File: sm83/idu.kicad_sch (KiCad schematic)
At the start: 48 parts

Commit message: SM83: Add schematic for interrupt handling
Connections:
- new net: IDU1. (CHAIN_A_~{Y}), IDU_MUX_L1.
- new net: IDU0. (ZERO_Y), IDU_MUX_L0.
- new net: IDU2. (CHAIN_A_~{Y}), IDU_MUX_L2.
- new net: IDU6. (CHAIN_A_~{Y}), IDU_MUX_H6.
- new net: IDU3. (CHAIN_A_~{Y}), IDU_MUX_L3.
- new net: IDU0. (ZERO_Y), IDU_MUX_L7.
- new net: IDU3. (CHAIN_A_~{Y}), IDU_MUX_H3.
- new net: IDU2. (CHAIN_A_~{Y}), IDU3. (CHAIN_A_~{Y}) (x2)
- new net: IDU3. (CHAIN_A_~{Y}), IDU4. (CHAIN_A_~{Y}) (x2)
- new net: IDU2. (CHAIN_A_~{Y}), IDU_MUX_H2.
- new net: IDU0. (ZERO_Y), IDU_MUX_H0.
- new net: IDU1. (CHAIN_A_~{Y}), IDU_MUX_H1.
- new net: IDU4. (CHAIN_A_~{Y}), IDU_MUX_L4.
- new net: IDU1. (CHAIN_A_~{Y}), IDU2. (CHAIN_A_~{Y}) (x2)
- new net: IDU6. (CHAIN_A_~{Y}), IDU_MUX_L6.
- new net: IDU0. (ZERO_Y), IDU1. (CHAIN_A_~{Y}) (x2)
- new net: IDU5. (CHAIN_A_~{Y}), IDU6. (CHAIN_A_~{Y}) (x2)
- new net: IDU6. (CHAIN_A_~{Y}), IDU7. (NOT_A_Y) (x2)
- new net: IDU4. (CHAIN_A_~{Y}), IDU_MUX_H4.
- new net: IDU4. (CHAIN_A_~{Y}), IDU5. (CHAIN_A_~{Y}) (x2)
- new net: IDU5. (CHAIN_A_~{Y}), IDU_MUX_H5.
- new net: IDU5. (CHAIN_A_~{Y}), IDU_MUX_L5.

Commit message: Finish SM83 CPU schematic
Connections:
- new net: IDU1. (CHAIN_A_~{Y}), IDU_MUX_L1.
- new net: IDU0. (ZERO_Y), IDU_MUX_L0.
- new net: IDU2. (CHAIN_A_~{Y}), IDU_MUX_L2.
- new net: IDU6. (CHAIN_A_~{Y}), IDU_MUX_H6.
- new net: IDU3. (CHAIN_A_~{Y}), IDU_MUX_L3.
- new net: IDU0. (ZERO_Y), IDU_MUX_L7.
- new net: IDU3. (CHAIN_A_~{Y}), IDU_MUX_H3.
- new net: IDU2. (CHAIN_A_~{Y}), IDU3. (CHAIN_A_~{Y}) (x2)
- new net: IDU3. (CHAIN_A_~{Y}), IDU4. (CHAIN_A_~{Y}) (x2)
- new net: IDU2. (CHAIN_A_~{Y}), IDU_MUX_H2.
- new net: IDU0. (ZERO_Y), IDU_MUX_H0.
- new net: IDU1. (CHAIN_A_~{Y}), IDU_MUX_H1.
- new net: IDU4. (CHAIN_A_~{Y}), IDU_MUX_L4.
- new net: IDU1. (CHAIN_A_~{Y}), IDU2. (CHAIN_A_~{Y}) (x2)
- new net: IDU6. (CHAIN_A_~{Y}), IDU_MUX_L6.
- new net: IDU0. (ZERO_Y), IDU1. (CHAIN_A_~{Y}) (x2)
- new net: IDU5. (CHAIN_A_~{Y}), IDU6. (CHAIN_A_~{Y}) (x2)
- new net: IDU6. (CHAIN_A_~{Y}), IDU7. (NOT_A_Y) (x2)
- new net: IDU4. (CHAIN_A_~{Y}), IDU_MUX_H4.
- new net: IDU4. (CHAIN_A_~{Y}), IDU5. (CHAIN_A_~{Y}) (x2)
- new net: IDU5. (CHAIN_A_~{Y}), IDU_MUX_H5.
- new net: IDU5. (CHAIN_A_~{Y}), IDU_MUX_L5.
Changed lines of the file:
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@@
 	(title_block
 		(title "SM83 CPU")
-		(date "2025-12-08")
+		(date "2025-12-24")
 		(rev "0")
 		(company "CC-BY-SA-4.0 Michael Singer")

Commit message: SM83: Merge dist. NANDs and NOR from IRQ_PRIOs
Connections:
- new net: IDU1. (CHAIN_A_~{Y}), IDU_MUX_L1.
- new net: IDU0. (ZERO_Y), IDU_MUX_L0.
- new net: IDU2. (CHAIN_A_~{Y}), IDU_MUX_L2.
- new net: IDU6. (CHAIN_A_~{Y}), IDU_MUX_H6.
- new net: IDU3. (CHAIN_A_~{Y}), IDU_MUX_L3.
- new net: IDU0. (ZERO_Y), IDU_MUX_L7.
- new net: IDU3. (CHAIN_A_~{Y}), IDU_MUX_H3.
- new net: IDU2. (CHAIN_A_~{Y}), IDU3. (CHAIN_A_~{Y}) (x2)
- new net: IDU3. (CHAIN_A_~{Y}), IDU4. (CHAIN_A_~{Y}) (x2)
- new net: IDU2. (CHAIN_A_~{Y}), IDU_MUX_H2.
- new net: IDU0. (ZERO_Y), IDU_MUX_H0.
- new net: IDU1. (CHAIN_A_~{Y}), IDU_MUX_H1.
- new net: IDU4. (CHAIN_A_~{Y}), IDU_MUX_L4.
- new net: IDU1. (CHAIN_A_~{Y}), IDU2. (CHAIN_A_~{Y}) (x2)
- new net: IDU6. (CHAIN_A_~{Y}), IDU_MUX_L6.
- new net: IDU0. (ZERO_Y), IDU1. (CHAIN_A_~{Y}) (x2)
- new net: IDU5. (CHAIN_A_~{Y}), IDU6. (CHAIN_A_~{Y}) (x2)
- new net: IDU6. (CHAIN_A_~{Y}), IDU7. (NOT_A_Y) (x2)
- new net: IDU4. (CHAIN_A_~{Y}), IDU_MUX_H4.
- new net: IDU4. (CHAIN_A_~{Y}), IDU5. (CHAIN_A_~{Y}) (x2)
- new net: IDU5. (CHAIN_A_~{Y}), IDU_MUX_H5.
- new net: IDU5. (CHAIN_A_~{Y}), IDU_MUX_L5.
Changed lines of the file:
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@@
 	(title_block
 		(title "SM83 CPU")
-		(date "2025-12-24")
+		(date "2025-12-25")
 		(rev "0")
 		(company "CC-BY-SA-4.0 Michael Singer")

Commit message: Release version 0.9 of both schematics
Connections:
- new net: IDU1. (CHAIN_A_~{Y}), IDU_MUX_L1.
- new net: IDU0. (ZERO_Y), IDU_MUX_L0.
- new net: IDU2. (CHAIN_A_~{Y}), IDU_MUX_L2.
- new net: IDU6. (CHAIN_A_~{Y}), IDU_MUX_H6.
- new net: IDU3. (CHAIN_A_~{Y}), IDU_MUX_L3.
- new net: IDU0. (ZERO_Y), IDU_MUX_L7.
- new net: IDU3. (CHAIN_A_~{Y}), IDU_MUX_H3.
- new net: IDU2. (CHAIN_A_~{Y}), IDU3. (CHAIN_A_~{Y}) (x2)
- new net: IDU3. (CHAIN_A_~{Y}), IDU4. (CHAIN_A_~{Y}) (x2)
- new net: IDU2. (CHAIN_A_~{Y}), IDU_MUX_H2.
- new net: IDU0. (ZERO_Y), IDU_MUX_H0.
- new net: IDU1. (CHAIN_A_~{Y}), IDU_MUX_H1.
- new net: IDU4. (CHAIN_A_~{Y}), IDU_MUX_L4.
- new net: IDU1. (CHAIN_A_~{Y}), IDU2. (CHAIN_A_~{Y}) (x2)
- new net: IDU6. (CHAIN_A_~{Y}), IDU_MUX_L6.
- new net: IDU0. (ZERO_Y), IDU1. (CHAIN_A_~{Y}) (x2)
- new net: IDU5. (CHAIN_A_~{Y}), IDU6. (CHAIN_A_~{Y}) (x2)
- new net: IDU6. (CHAIN_A_~{Y}), IDU7. (NOT_A_Y) (x2)
- new net: IDU4. (CHAIN_A_~{Y}), IDU_MUX_H4.
- new net: IDU4. (CHAIN_A_~{Y}), IDU5. (CHAIN_A_~{Y}) (x2)
- new net: IDU5. (CHAIN_A_~{Y}), IDU_MUX_H5.
- new net: IDU5. (CHAIN_A_~{Y}), IDU_MUX_L5.
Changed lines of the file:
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@@
 		(title "SM83 CPU")
 		(date "2025-12-25")
-		(rev "0")
+		(rev "0.9")
 		(company "CC-BY-SA-4.0 Michael Singer")
 		(comment 1 "https://github.com/msinger/dmg-schematics")

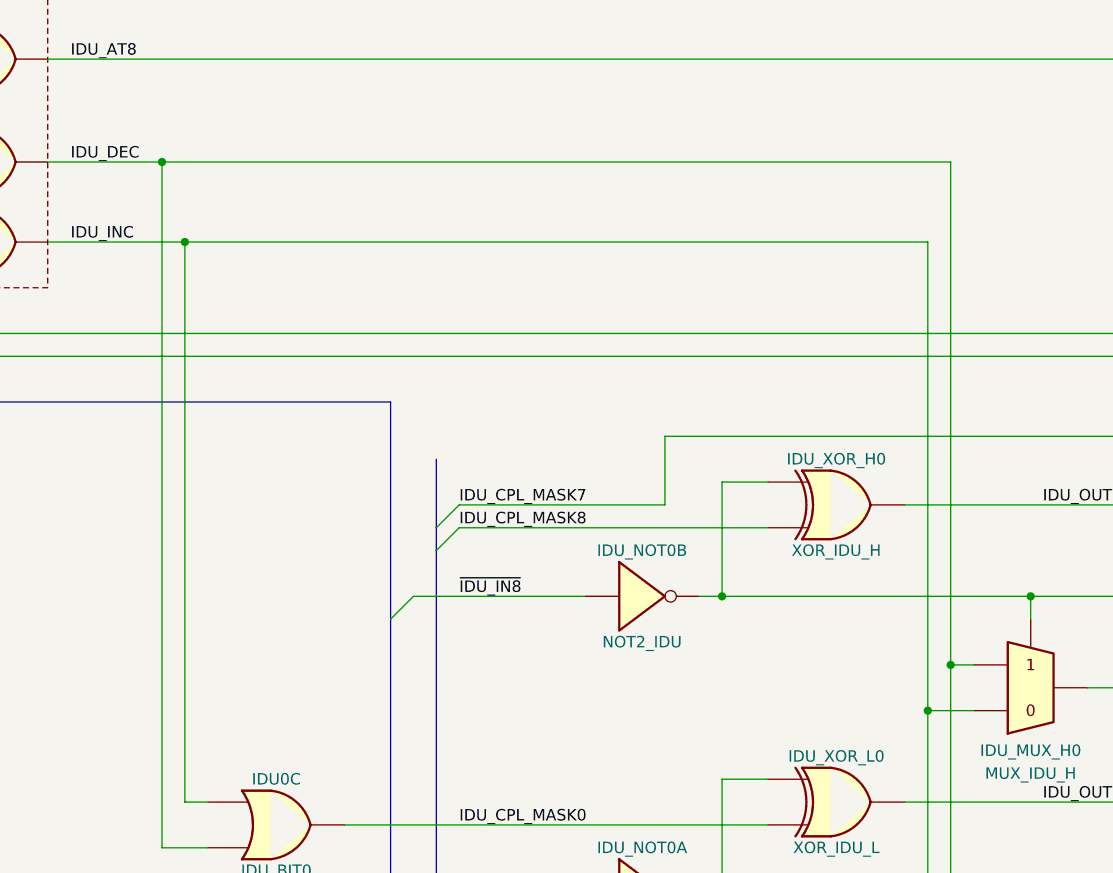
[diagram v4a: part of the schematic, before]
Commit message: SM83: Small IDU fixes
* IDU_INC and IDU_DEC signals were swapped at muxer inputs.
* ~{IDU_IN[0..15]} was missing ~{} in some places.
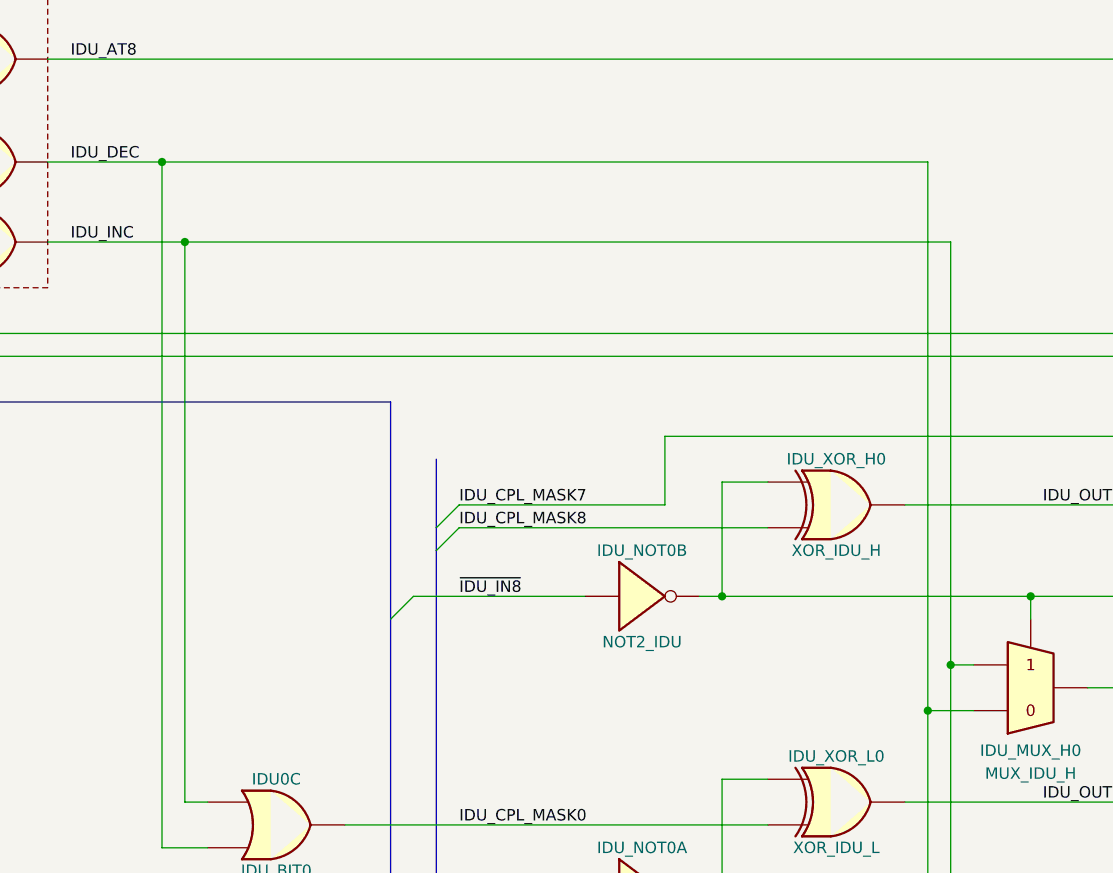
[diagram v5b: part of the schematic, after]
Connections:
- new net: IDU1. (CHAIN_A_~{Y}), IDU_MUX_L1.
- new net: IDU0. (ZERO_Y), IDU_MUX_L0.
- new net: IDU2. (CHAIN_A_~{Y}), IDU_MUX_L2.
- new net: IDU6. (CHAIN_A_~{Y}), IDU_MUX_H6.
- new net: IDU3. (CHAIN_A_~{Y}), IDU_MUX_L3.
- new net: IDU0. (ZERO_Y), IDU_MUX_L7.
- new net: IDU3. (CHAIN_A_~{Y}), IDU_MUX_H3.
- new net: IDU2. (CHAIN_A_~{Y}), IDU3. (CHAIN_A_~{Y}) (x2)
- new net: IDU3. (CHAIN_A_~{Y}), IDU4. (CHAIN_A_~{Y}) (x2)
- new net: IDU2. (CHAIN_A_~{Y}), IDU_MUX_H2.
- new net: IDU0. (ZERO_Y), IDU_MUX_H0.
- new net: IDU1. (CHAIN_A_~{Y}), IDU_MUX_H1.
- new net: IDU4. (CHAIN_A_~{Y}), IDU_MUX_L4.
- new net: IDU1. (CHAIN_A_~{Y}), IDU2. (CHAIN_A_~{Y}) (x2)
- new net: IDU6. (CHAIN_A_~{Y}), IDU_MUX_L6.
- new net: IDU0. (ZERO_Y), IDU1. (CHAIN_A_~{Y}) (x2)
- new net: IDU5. (CHAIN_A_~{Y}), IDU6. (CHAIN_A_~{Y}) (x2)
- new net: IDU6. (CHAIN_A_~{Y}), IDU7. (NOT_A_Y) (x2)
- new net: IDU4. (CHAIN_A_~{Y}), IDU_MUX_H4.
- new net: IDU4. (CHAIN_A_~{Y}), IDU5. (CHAIN_A_~{Y}) (x2)
- new net: IDU5. (CHAIN_A_~{Y}), IDU_MUX_H5.
- new net: IDU5. (CHAIN_A_~{Y}), IDU_MUX_L5.
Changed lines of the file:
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@@
 	)
 	(junction
-		(at 292.1 134.62)
-		(diameter 0)
-		(color 0 0 0 0)
-	)
-	(junction
 		(at 328.93 443.23)
 		(diameter 0)
@@
 	)
 	(junction
+		(at 292.1 134.62)
+		(diameter 0)
+		(color 0 0 0 0)
+	)
+	(junction
 		(at 292.1 670.56)
 		(diameter 0)
@@
 	)
 	(junction
+		(at 289.56 139.7)
+		(diameter 0)
+		(color 0 0 0 0)
+	)
+	(junction
 		(at 328.93 191.77)
 		(diameter 0)
@@
 	)
 	(junction
-		(at 289.56 139.7)
-		(diameter 0)
-		(color 0 0 0 0)
-	)
-	(junction
 		(at 328.93 527.05)
 		(diameter 0)
@@
 	(wire
 		(pts
-			(xy 289.56 139.7) (xy 289.56 87.63)
-		)
-		(stroke
-			(width 0)
-			(type default)
-		)
-	)
-	(wire
-		(pts
 			(xy 292.1 335.28) (xy 292.1 386.08)
 		)
@@
 	(wire
 		(pts
-			(xy 289.56 87.63) (xy 207.01 87.63)
+			(xy 207.01 87.63) (xy 292.1 87.63)
 		)
 		(stroke
@@
 	(wire
 		(pts
-			(xy 292.1 78.74) (xy 292.1 134.62)
-		)
-		(stroke
-			(width 0)
-			(type default)
-		)
-	)
-	(wire
-		(pts
 			(xy 372.11 520.7) (xy 331.47 520.7)
 		)
@@
 	(wire
 		(pts
+			(xy 292.1 87.63) (xy 292.1 134.62)
+		)
+		(stroke
+			(width 0)
+			(type default)
+		)
+	)
+	(wire
+		(pts
 			(xy 316.23 246.38) (xy 316.23 254)
 		)
@@
 	(wire
 		(pts
+			(xy 289.56 139.7) (xy 289.56 78.74)
+		)
+		(stroke
+			(width 0)
+			(type default)
+		)
+	)
+	(wire
+		(pts
 			(xy 266.7 127) (xy 300.99 127)
 		)
@@
 	(wire
 		(pts
-			(xy 204.47 78.74) (xy 292.1 78.74)
+			(xy 204.47 78.74) (xy 289.56 78.74)
 		)
 		(stroke

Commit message: Release revision 0.10 of both schematics
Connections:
- new net: IDU1. (CHAIN_A_~{Y}), IDU_MUX_L1.
- new net: IDU0. (ZERO_Y), IDU_MUX_L0.
- new net: IDU2. (CHAIN_A_~{Y}), IDU_MUX_L2.
- new net: IDU6. (CHAIN_A_~{Y}), IDU_MUX_H6.
- new net: IDU3. (CHAIN_A_~{Y}), IDU_MUX_L3.
- new net: IDU0. (ZERO_Y), IDU_MUX_L7.
- new net: IDU3. (CHAIN_A_~{Y}), IDU_MUX_H3.
- new net: IDU2. (CHAIN_A_~{Y}), IDU3. (CHAIN_A_~{Y}) (x2)
- new net: IDU3. (CHAIN_A_~{Y}), IDU4. (CHAIN_A_~{Y}) (x2)
- new net: IDU2. (CHAIN_A_~{Y}), IDU_MUX_H2.
- new net: IDU0. (ZERO_Y), IDU_MUX_H0.
- new net: IDU1. (CHAIN_A_~{Y}), IDU_MUX_H1.
- new net: IDU4. (CHAIN_A_~{Y}), IDU_MUX_L4.
- new net: IDU1. (CHAIN_A_~{Y}), IDU2. (CHAIN_A_~{Y}) (x2)
- new net: IDU6. (CHAIN_A_~{Y}), IDU_MUX_L6.
- new net: IDU0. (ZERO_Y), IDU1. (CHAIN_A_~{Y}) (x2)
- new net: IDU5. (CHAIN_A_~{Y}), IDU6. (CHAIN_A_~{Y}) (x2)
- new net: IDU6. (CHAIN_A_~{Y}), IDU7. (NOT_A_Y) (x2)
- new net: IDU4. (CHAIN_A_~{Y}), IDU_MUX_H4.
- new net: IDU4. (CHAIN_A_~{Y}), IDU5. (CHAIN_A_~{Y}) (x2)
- new net: IDU5. (CHAIN_A_~{Y}), IDU_MUX_H5.
- new net: IDU5. (CHAIN_A_~{Y}), IDU_MUX_L5.
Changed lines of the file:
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@@
 	(title_block
 		(title "SM83 CPU")
-		(date "2025-12-25")
-		(rev "0.9")
+		(date "2026-03-22")
+		(rev "0.10")
 		(company "CC-BY-SA-4.0 Michael Singer")
 		(comment 1 "https://github.com/msinger/dmg-schematics")
@@
 		)
 		(instances
-			(project ""
+			(project "sm83"
 				(path "/8717d046-1dfd-46fe-a5f7-4e4d2f07de68/96f424a6-eb9c-4685-8465-2aab0d38a576"
 					(reference "IDU_XOR_L0")
@@
 		)
 		(instances
-			(project ""
+			(project "sm83"
 				(path "/8717d046-1dfd-46fe-a5f7-4e4d2f07de68/96f424a6-eb9c-4685-8465-2aab0d38a576"
 					(reference "IDU_CTL")
@@
 		)
 		(instances
-			(project ""
+			(project "sm83"
 				(path "/8717d046-1dfd-46fe-a5f7-4e4d2f07de68/96f424a6-eb9c-4685-8465-2aab0d38a576"
 					(reference "IDU0")
@@
 		)
 		(instances
-			(project ""
+			(project "sm83"
 				(path "/8717d046-1dfd-46fe-a5f7-4e4d2f07de68/96f424a6-eb9c-4685-8465-2aab0d38a576"
 					(reference "IDU7")
@@
 		)
 		(instances
-			(project ""
+			(project "sm83"
 				(path "/8717d046-1dfd-46fe-a5f7-4e4d2f07de68/96f424a6-eb9c-4685-8465-2aab0d38a576"
 					(reference "IDU_XOR_H0")
@@
 		)
 		(instances
-			(project ""
+			(project "sm83"
 				(path "/8717d046-1dfd-46fe-a5f7-4e4d2f07de68/96f424a6-eb9c-4685-8465-2aab0d38a576"
 					(reference "IDU1")
@@
 		)
 		(instances
-			(project ""
+			(project "sm83"
 				(path "/8717d046-1dfd-46fe-a5f7-4e4d2f07de68/96f424a6-eb9c-4685-8465-2aab0d38a576"
 					(reference "IDU0")
@@
 		)
 		(instances
-			(project ""
+			(project "sm83"
 				(path "/8717d046-1dfd-46fe-a5f7-4e4d2f07de68/96f424a6-eb9c-4685-8465-2aab0d38a576"
 					(reference "IDU1")
@@
 		)
 		(instances
-			(project ""
+			(project "sm83"
 				(path "/8717d046-1dfd-46fe-a5f7-4e4d2f07de68/96f424a6-eb9c-4685-8465-2aab0d38a576"
 					(reference "IDU7")

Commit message: Release revision 0.11 of both schematics
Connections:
- new net: IDU1. (CHAIN_A_~{Y}), IDU_MUX_L1.
- new net: IDU0. (ZERO_Y), IDU_MUX_L0.
- new net: IDU2. (CHAIN_A_~{Y}), IDU_MUX_L2.
- new net: IDU6. (CHAIN_A_~{Y}), IDU_MUX_H6.
- new net: IDU3. (CHAIN_A_~{Y}), IDU_MUX_L3.
- new net: IDU0. (ZERO_Y), IDU_MUX_L7.
- new net: IDU3. (CHAIN_A_~{Y}), IDU_MUX_H3.
- new net: IDU2. (CHAIN_A_~{Y}), IDU3. (CHAIN_A_~{Y}) (x2)
- new net: IDU3. (CHAIN_A_~{Y}), IDU4. (CHAIN_A_~{Y}) (x2)
- new net: IDU2. (CHAIN_A_~{Y}), IDU_MUX_H2.
- new net: IDU0. (ZERO_Y), IDU_MUX_H0.
- new net: IDU1. (CHAIN_A_~{Y}), IDU_MUX_H1.
- new net: IDU4. (CHAIN_A_~{Y}), IDU_MUX_L4.
- new net: IDU1. (CHAIN_A_~{Y}), IDU2. (CHAIN_A_~{Y}) (x2)
- new net: IDU6. (CHAIN_A_~{Y}), IDU_MUX_L6.
- new net: IDU0. (ZERO_Y), IDU1. (CHAIN_A_~{Y}) (x2)
- new net: IDU5. (CHAIN_A_~{Y}), IDU6. (CHAIN_A_~{Y}) (x2)
- new net: IDU6. (CHAIN_A_~{Y}), IDU7. (NOT_A_Y) (x2)
- new net: IDU4. (CHAIN_A_~{Y}), IDU_MUX_H4.
- new net: IDU4. (CHAIN_A_~{Y}), IDU5. (CHAIN_A_~{Y}) (x2)
- new net: IDU5. (CHAIN_A_~{Y}), IDU_MUX_H5.
- new net: IDU5. (CHAIN_A_~{Y}), IDU_MUX_L5.
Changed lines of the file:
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@@
 	(title_block
 		(title "SM83 CPU")
-		(date "2026-03-22")
-		(rev "0.10")
+		(date "2026-04-11")
+		(rev "0.11")
 		(company "CC-BY-SA-4.0 Michael Singer")
 		(comment 1 "https://github.com/msinger/dmg-schematics")
